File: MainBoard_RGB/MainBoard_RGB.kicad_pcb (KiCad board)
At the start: 2 copper layers, 33.3 x 26.1 mm, 35 parts, among them J1 Conn_01x02_Female, J2 Conn_02x03_Top_Bottom, J3 Conn_01x04_Female, Q1 Q_NMOS_DGS, Q2 Q_NMOS_DGS, Q3 Q_NMOS_DGS, U1 ESP-01v090, U2 AZ1117-3.3, U3 ATTINY85-20PU

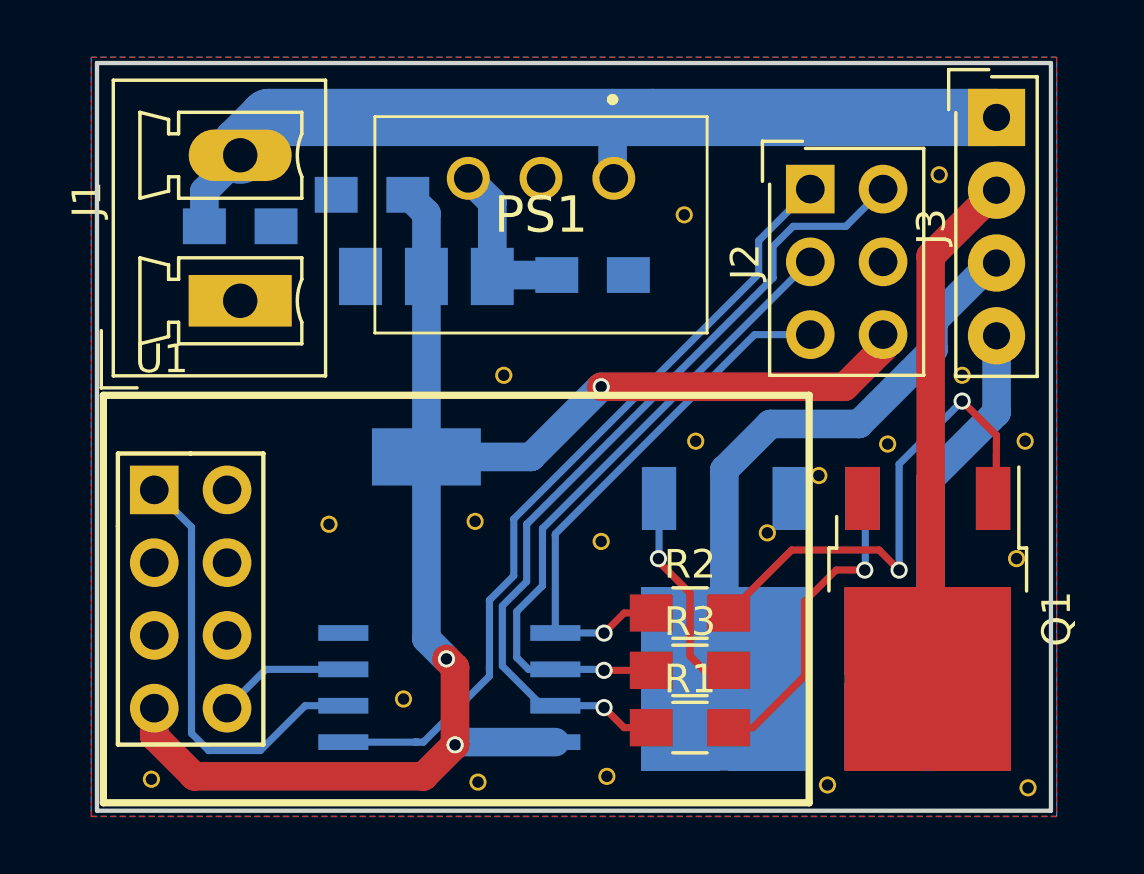
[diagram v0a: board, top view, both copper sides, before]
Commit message: RGB and Relay platform finished
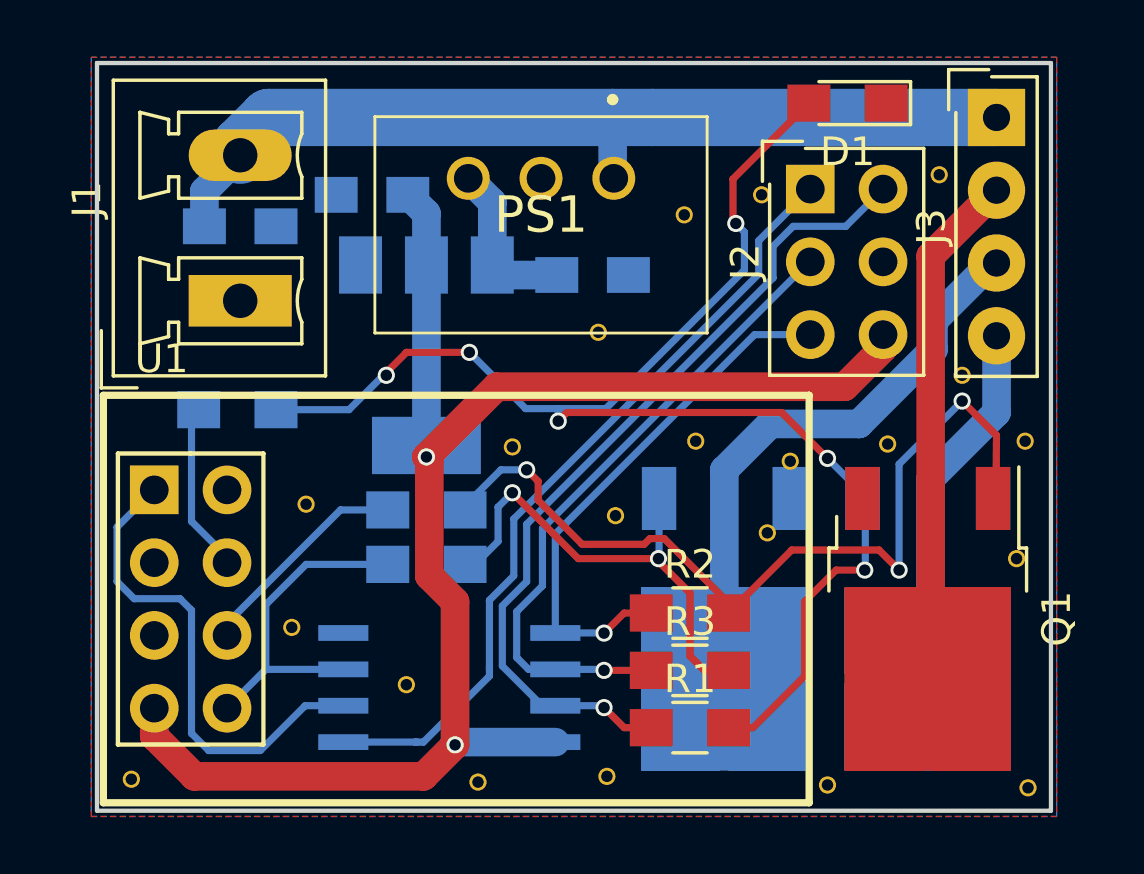
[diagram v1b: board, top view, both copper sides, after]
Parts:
- removed the REF** at (130.0, 113.4)
- added D1: LED, LEDs:LED_0805_HandSoldering, F.Cu at (145.5, 92.6)
- added R4: 1k, Resistors_SMD:R_0805_HandSoldering, B.Cu at (124.2, 103.3)
- added R5: 1k, Resistors_SMD:R_0805_HandSoldering, B.Cu at (130.8, 108.7)
- added R6: 1k, Resistors_SMD:R_0805_HandSoldering, B.Cu at (130.8, 106.8)
- added REF**: VIA-.4mm, VIA-.6mm, F.Cu at (133.8, 104.6)
- added REF**: VIA-.4mm, VIA-.6mm, F.Cu at (126.1, 110.9)
- added REF**: VIA-.4mm, VIA-.6mm, F.Cu at (130.1, 112.9)
- Q1, Q2, Q3: value Q_NMOS_DGS -> Q_NMOS_GDS
- moved REF** 15.2 mm to (142.5, 95.8)
- moved REF** 3.62 mm to (136.8, 100.6)
- moved REF** 1.12 mm to (143.5, 105.1)
- moved REF** 1.06 mm to (126.6, 106.6)
- moved REF** 1.03 mm to (137.4, 107.0)
- moved REF** 0.70 mm to (120.5, 116.2)
- moved U2 0.40 mm to (130.8, 101.4)
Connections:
- U2 pad 4: +3V3 -> (no net)
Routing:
- net /B_G: track 11.1 -> 50.9 mm, vias 1 -> 6
- net /R_G: track 17.9 -> 31.1 mm, vias 2 -> 3
- net /G_G: track 7.52 -> 17.0 mm, vias 1 -> 2
- net Net-(R6-Pad1): track 0.00 -> 7.67 mm
- net Net-(R5-Pad1): track 4.62 -> 11.7 mm
- net Net-(R4-Pad1): track 0.00 -> 5.96 mm
- net Net-(U1-Pad1): track 15.2 -> 17.2 mm
- net +3V3: vias 3 -> 2
